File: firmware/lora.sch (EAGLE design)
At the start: 24 parts, among them J1 SWD_PTH_SHROUD, X1 SMA-142-0701-801/806

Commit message: some nudging
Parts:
- removed U$5: BUS-SMA, Ava:BUS-SMA
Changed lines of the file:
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@@
 <part name="GND17" library="supply1" deviceset="GND" device=""/>
 <part name="GND18" library="supply1" deviceset="GND" device=""/>
-<part name="U$5" library="Ava" deviceset="BUS-SMA" device=""/>
 </parts>
 <sheets>
@@
 <instance part="GND17" gate="1" x="134.62" y="116.84" rot="R90"/>
 <instance part="GND18" gate="1" x="134.62" y="111.76" rot="R90"/>
-<instance part="U$5" gate="G$1" x="119.38" y="134.62" rot="MR0"/>
 </instances>
 <busses>

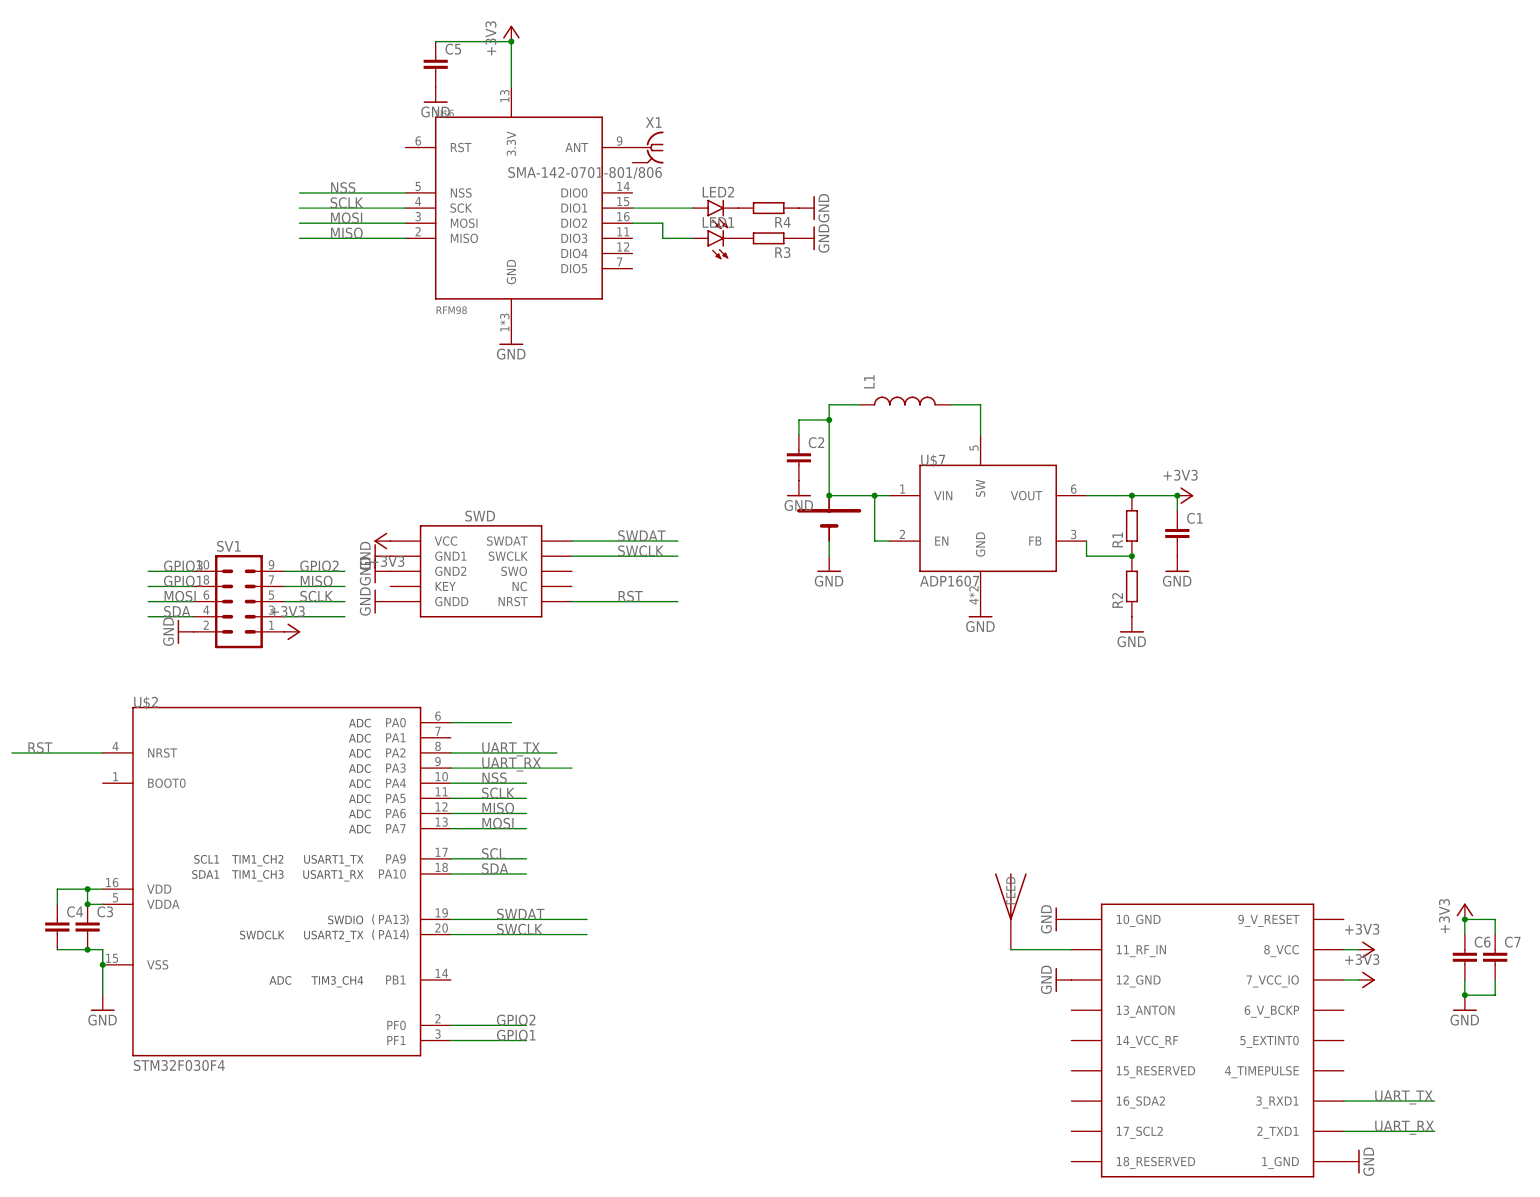
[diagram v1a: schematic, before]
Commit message: added esd diodes and supply reading
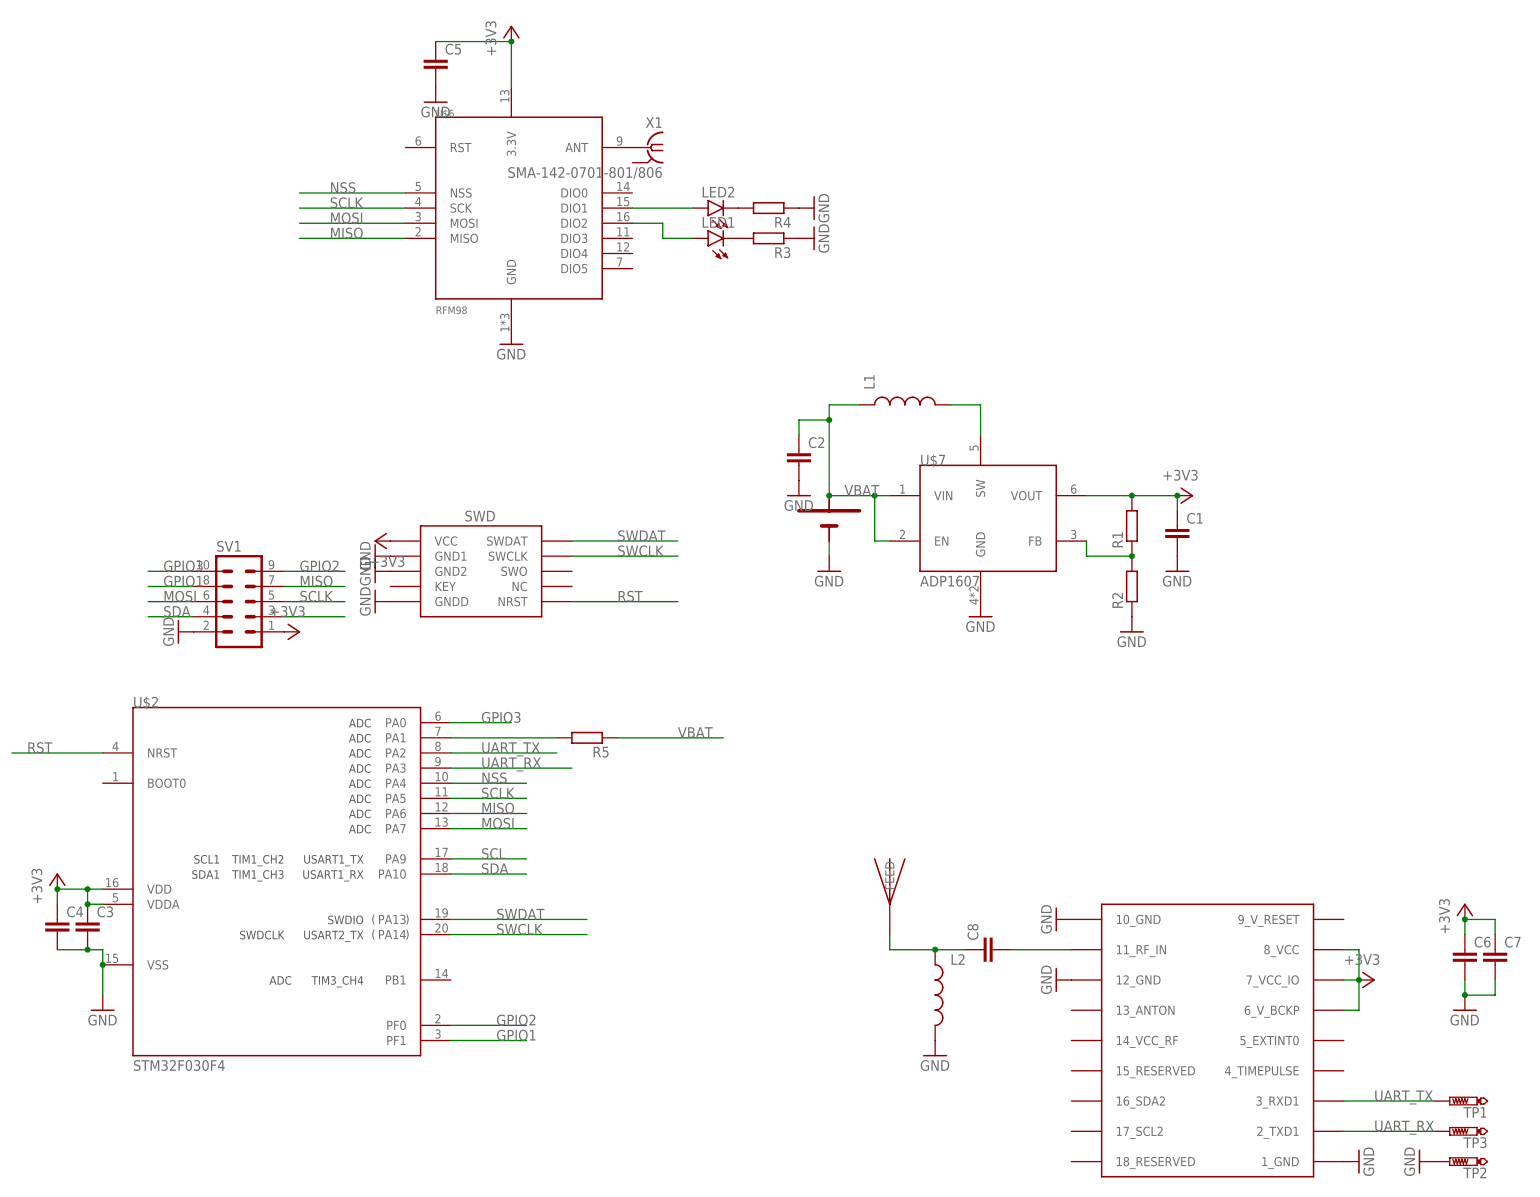
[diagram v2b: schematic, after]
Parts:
- added C8: (no value), rcl:C-EUC0603
- added L2: (no value), SparkFun-Passives:INDUCTOR0603
- added R5: (no value), rcl:R-EU_R0603
- added TP1, TP2, TP3: PTR1B1,27, testpad:PTR1B1,27
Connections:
- removed net N$11: C3.1, C4.1, U$2.VDD, U$2.VDDA
- new net N$9: R5.2, U$2.PA1
- new net VBAT: C2.1, L1.1, R5.1, U$1.+, U$7.EN, U$7.VIN
- net +3V3: now also C3.1, C4.1, U$2.VDD, U$2.VDDA, U$3.6_V_BCKP
- net GND: now also L2.2, TP2.TP
- net N$1: now also C8.2; no longer U$4.FEED
- net N$4: now also C8.1, L2.1, U$4.FEED; no longer C2.1, L1.1, U$1.+, U$7.EN, U$7.VIN
- net UART_RX: now also TP3.TP
- net UART_TX: now also TP1.TP
